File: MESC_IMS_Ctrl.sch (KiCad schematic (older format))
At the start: 70 parts, among them J1 Conn_01x08_Female, J10 Conn_01x04_Male, J2 Conn_01x08_Female, J3 Conn_01x08_Female, J4 Conn_01x06_Male, J5 Conn_ARM_JTAG_SWD_10, J6 USB_C_Receptacle_USB2.0, J7 Conn_01x03_Male, J8 Conn_01x04_Male, J9 Conn_01x08_Male, U1 STM32F303CBTx, Y1 ASE-8.000MHZ-LC-T

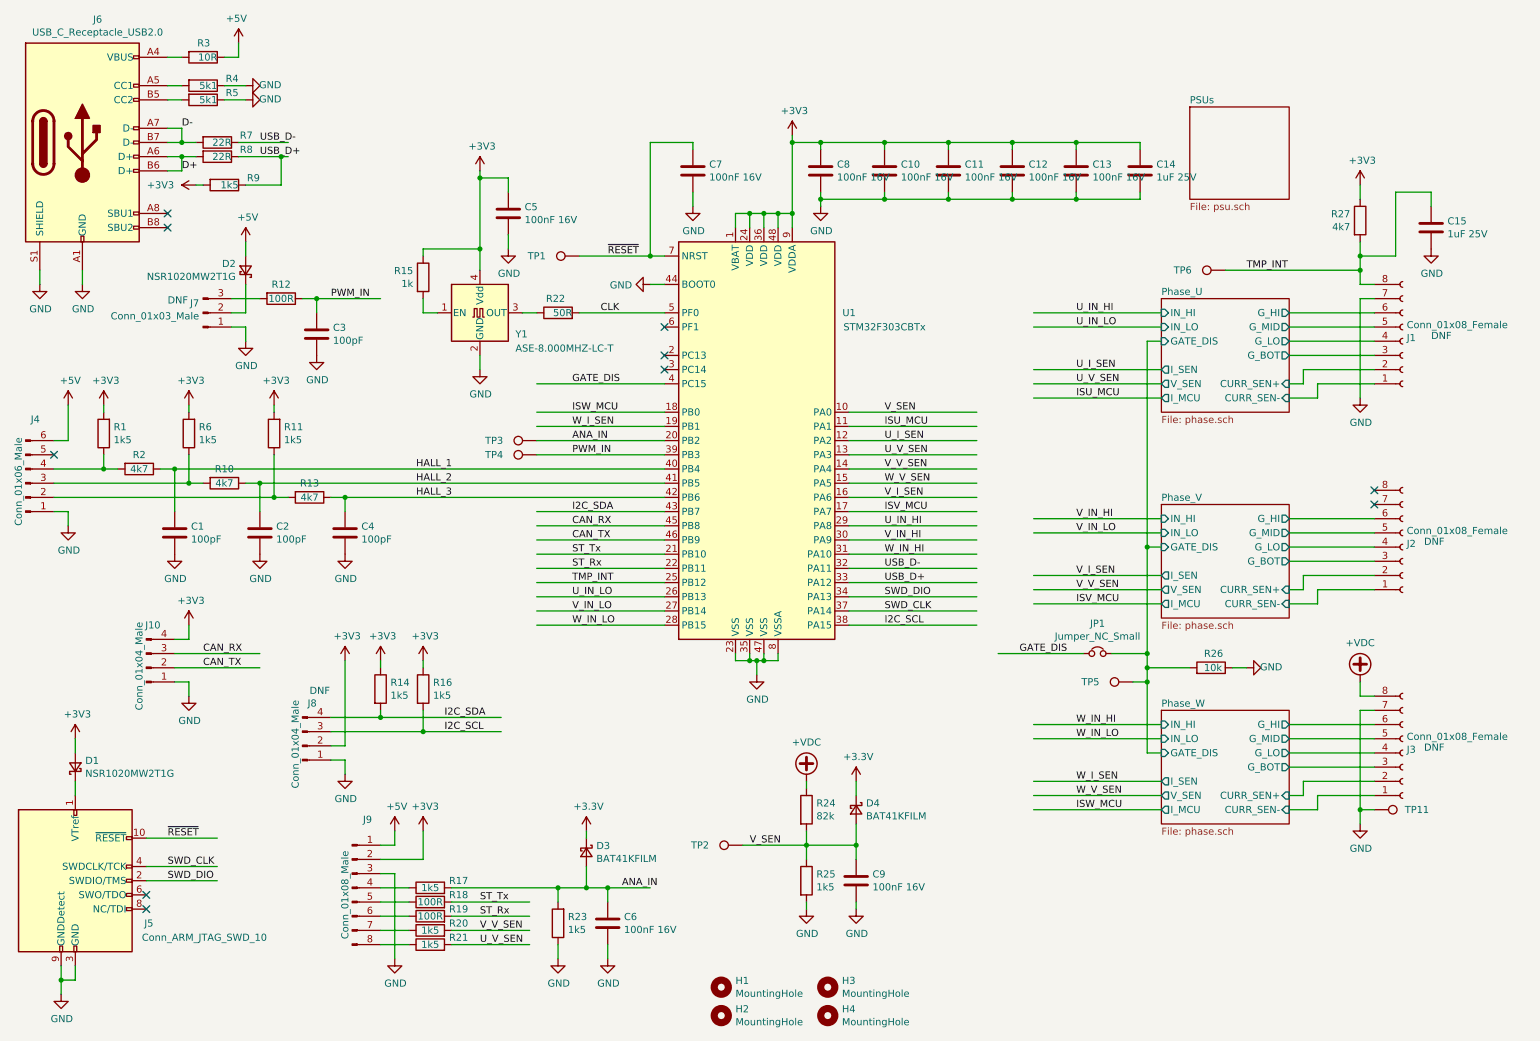
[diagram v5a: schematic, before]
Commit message: upgrading to 4layer
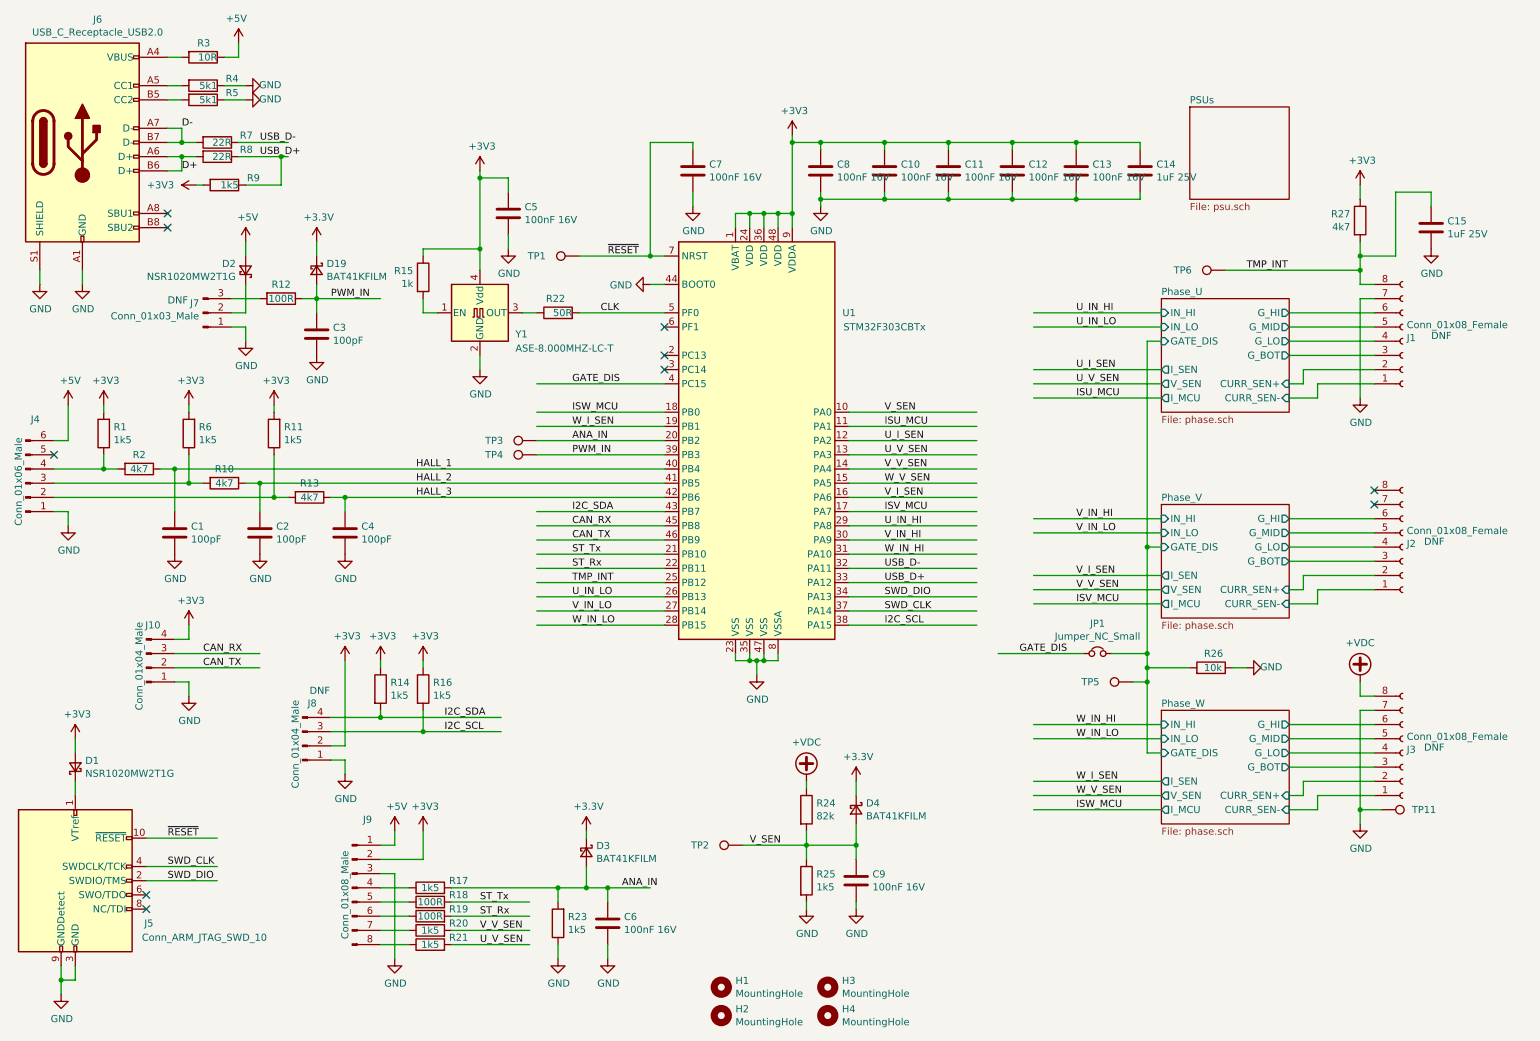
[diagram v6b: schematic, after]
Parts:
- added D19: BAT41KFILM, Diode_SMD:D_SOD-523, symbol Device:D_Schottky_Small
- TP1, TP11, TP2, TP3, TP4, TP5, TP6: footprint TestPoint:TestPoint_Pad_D1.5mm -> TestPoint:TestPoint_Pad_D1.0mm
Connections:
- wire segments 289 -> 291
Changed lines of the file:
@@
 	9550 2950 10150 2950
-Wire Wire Line
-	10050 5450 10050 6150
 Wire Wire Line
 	10150 5850 9550 5850
@@
 Wire Wire Line
 	10050 2250 10050 2350
-Wire Wire Line
-	5150 3150 4250 3150
-Text Label 4500 3150 0    50   ~ 0
-GATE_DIS
 Wire Wire Line
 	8650 2850 8550 2850
@@
 F 0 "TP6" V 9100 2650 50  0000 C CNN
 F 1 "TestPoint" V 9204 2422 50  0001 C CNN
-F 2 "TestPoint:TestPoint_Pad_D1.5mm" H 9300 2350 50  0001 C CNN
+F 2 "TestPoint:TestPoint_Pad_D1.0mm" H 9300 2350 50  0001 C CNN
 F 3 "~" H 9300 2350 50  0001 C CNN
 F 4 "~" H 9100 2350 50  0001 C CNN "LCSC"
@@
 F 0 "TP2" V 5700 6700 50  0000 C CNN
 F 1 "TestPoint" V 5804 6472 50  0001 C CNN
-F 2 "TestPoint:TestPoint_Pad_D1.5mm" H 5900 6400 50  0001 C CNN
+F 2 "TestPoint:TestPoint_Pad_D1.0mm" H 5900 6400 50  0001 C CNN
 F 3 "~" H 5900 6400 50  0001 C CNN
 F 4 "~" H 5700 6400 50  0001 C CNN "LCSC"
@@
 F 0 "TP5" V 8450 5550 50  0000 C CNN
 F 1 "TestPoint" V 8554 5322 50  0001 C CNN
-F 2 "TestPoint:TestPoint_Pad_D1.5mm" H 8650 5250 50  0001 C CNN
+F 2 "TestPoint:TestPoint_Pad_D1.0mm" H 8650 5250 50  0001 C CNN
 F 3 "~" H 8650 5250 50  0001 C CNN
 F 4 "~" H 8450 5250 50  0001 C CNN "LCSC"
@@
 F 0 "TP4" V 4250 3950 50  0000 C CNN
 F 1 "TestPoint" V 4354 3722 50  0001 C CNN
-F 2 "TestPoint:TestPoint_Pad_D1.5mm" H 4450 3650 50  0001 C CNN
+F 2 "TestPoint:TestPoint_Pad_D1.0mm" H 4450 3650 50  0001 C CNN
 F 3 "~" H 4450 3650 50  0001 C CNN
 F 4 "~" H 4250 3650 50  0001 C CNN "LCSC"
@@
 F 0 "TP3" V 4250 3850 50  0000 C CNN
 F 1 "TestPoint" V 4354 3622 50  0001 C CNN
-F 2 "TestPoint:TestPoint_Pad_D1.5mm" H 4450 3550 50  0001 C CNN
+F 2 "TestPoint:TestPoint_Pad_D1.0mm" H 4450 3550 50  0001 C CNN
 F 3 "~" H 4450 3550 50  0001 C CNN
 F 4 "~" H 4250 3550 50  0001 C CNN "LCSC"
@@
 F 0 "TP1" V 4550 2550 50  0000 C CNN
 F 1 "TestPoint" V 4654 2322 50  0001 C CNN
-F 2 "TestPoint:TestPoint_Pad_D1.5mm" H 4750 2250 50  0001 C CNN
+F 2 "TestPoint:TestPoint_Pad_D1.0mm" H 4750 2250 50  0001 C CNN
 F 3 "~" H 4750 2250 50  0001 C CNN
 F 4 "~" H 4550 2250 50  0001 C CNN "LCSC"
@@
 	0    1    1    0
 $EndComp
+Text Label 4500 3150 0    50   ~ 0
+GATE_DIS
+Wire Wire Line
+	5150 3150 4250 3150
+Wire Wire Line
+	10050 5450 10050 6150
+$Comp
+L Device:D_Schottky_Small D?
+U 1 1 609FDE63
+P 2700 2350
+AR Path="/6070CE7F/609FDE63" Ref="D?"  Part="1"
+AR Path="/6074FE4E/609FDE63" Ref="D?"  Part="1"
+AR Path="/6075047A/609FDE63" Ref="D?"  Part="1"
+AR Path="/609FDE63" Ref="D19"  Part="1"
+F 0 "D19" V 2654 2420 50  0000 L CNN
+F 1 "BAT41KFILM" V 2745 2420 50  0000 L CNN
+F 2 "Diode_SMD:D_SOD-523" V 2700 2350 50  0001 C CNN
+F 3 "~" V 2700 2350 50  0001 C CNN
+F 4 "C73150" H 2700 2350 50  0001 C CNN "LCSC"
+F 5 "Yes" H 2700 2350 50  0001 C CNN "Checked"
+	1    2700 2350
+	0    1    1    0
+$EndComp
+$Comp
+L power:+3.3V #PWR?
+U 1 1 609FDE6A
+P 2700 2150
+AR Path="/6070CE7F/609FDE6A" Ref="#PWR?"  Part="1"
+AR Path="/607145EC/609FDE6A" Ref="#PWR?"  Part="1"
+AR Path="/60714740/609FDE6A" Ref="#PWR?"  Part="1"
+AR Path="/6074FE4E/609FDE6A" Ref="#PWR?"  Part="1"
+AR Path="/6075047A/609FDE6A" Ref="#PWR?"  Part="1"
+AR Path="/609FDE6A" Ref="#PWR060"  Part="1"
+F 0 "#PWR060" H 2700 2000 50  0001 C CNN
+F 1 "+3.3V" H 2715 2323 50  0000 C CNN
+F 2 "" H 2700 2150 50  0001 C CNN
+F 3 "" H 2700 2150 50  0001 C CNN
+	1    2700 2150
+	1    0    0    -1
+$EndComp
+Wire Wire Line
+	2700 2150 2700 2250
+Wire Wire Line
+	2700 2450 2700 2550
 $Comp
 L Connector:TestPoint TP11
-U 1 1 609AA071
-P 10150 6150
-F 0 "TP11" V 10150 6450 50  0000 C CNN
-F 1 "TestPoint" V 10254 6222 50  0001 C CNN
-F 2 "TestPoint:TestPoint_Pad_D1.5mm" H 10350 6150 50  0001 C CNN
-F 3 "~" H 10350 6150 50  0001 C CNN
-F 4 "~" H 10150 6150 50  0001 C CNN "LCSC"
-F 5 "Yes" H 10150 6150 50  0001 C CNN "Checked"
-	1    10150 6150
+U 1 1 60A80FB1
+P 10200 6150
+F 0 "TP11" V 10200 6450 50  0000 C CNN
+F 1 "TestPoint" V 10304 6222 50  0001 C CNN
+F 2 "TestPoint:TestPoint_Pad_D1.0mm" H 10400 6150 50  0001 C CNN
+F 3 "~" H 10400 6150 50  0001 C CNN
+F 4 "~" H 10200 6150 50  0001 C CNN "LCSC"
+F 5 "Yes" H 10200 6150 50  0001 C CNN "Checked"
+	1    10200 6150
 	0    1    -1   0
 $EndComp
 Wire Wire Line
-	10150 6150 10050 6150
+	10200 6150 10050 6150
 Connection ~ 10050 6150
 Wire Wire Line
